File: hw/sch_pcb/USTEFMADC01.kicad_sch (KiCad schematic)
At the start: 34 parts, among them J1 3.3 or 5V, J1001 HEADER_2x10, J9 MCX, M1 RFShield_TwoPieces, U2 OPA314, U3 ISL21080CIH330Z-TK, U4 LTC1865-MS, U5 OPA314

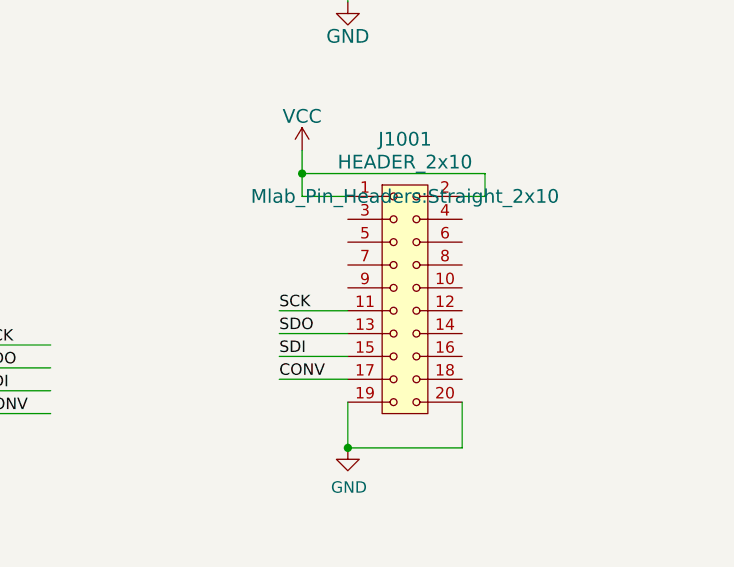
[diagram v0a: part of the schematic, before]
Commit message: Update to KiCAD 10. Fix component UST_IDs.
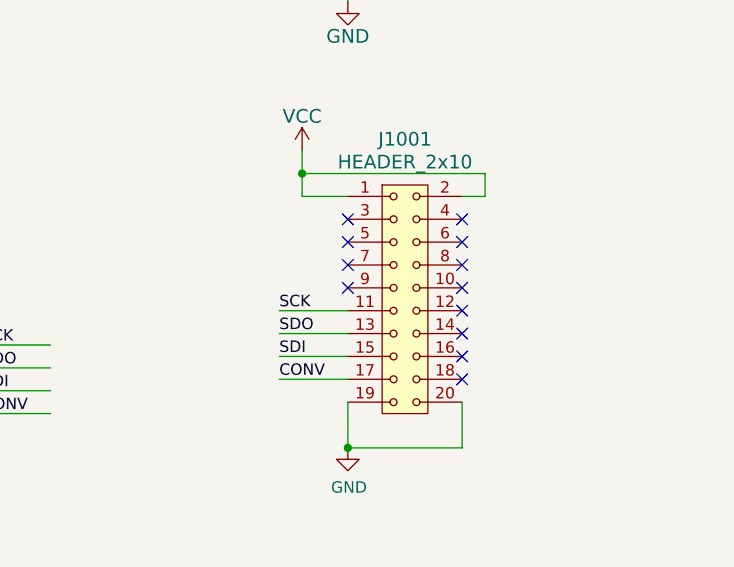
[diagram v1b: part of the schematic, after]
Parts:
- C1, C11, C3: UST_ID 6508260b462c6d9e720541f1 -> 5c70984712875079b91f8b4c
- C2: UST_ID 6508260b462c6d9e720541f1 -> 5c70984712875079b91f8b49
- C4: UST_ID 5c70984812875079b91f8ba6 -> 5c70984712875079b91f8b49
- R1: UST_ID 5c70984712875079b91f8b6d -> 5c70984712875079b91f8aa0
- R2: UST_ID 5c70984512875079b91f895e -> 5c70984612875079b91f8993
- R3: UST_ID 5c70984512875079b91f8962 -> 5c70984712875079b91f8a8a
- R8, R9: UST_ID 5c70984712875079b91f8b6d -> 5c70984512875079b91f898c
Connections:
- no-connect marks 0 -> 12
